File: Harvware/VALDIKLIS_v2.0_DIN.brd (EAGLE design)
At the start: 100 x 86.4 mm, 56 parts, among them IC1 ATMEGA1284, J1 6-3.50, J10 6-3.50, J2 6-3.50, J3 6-3.50, J4 4-3.50, J5 2-3.50, J6 4-3.50, J7 4-3.50, J8 4-3.50, J9 6-3.50, K1 G5V1, K2 G5V1, K3 G5V1, K4 G5V1, Q3 TIP120V, Q4 TIP120V, X12 12MHZ, Y2 16MHz

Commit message: 1
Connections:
- net 0(RX0) renamed D8(RX0)
- net 1(TX0) renamed D9(TX0)
- net 11(MOSI) renamed D5(MOSI)
- net 12(MISO) renamed D6(MISO)
- net 13(SCK) renamed D7(SCK)
- net 16(TDI) renamed D21(TDI)
- net 17(TDO) renamed D20(TDO)
- net 18(TMS) renamed D19(TMS)
- net 19(TCK) renamed D18(TCK)
- net 2(RX1) renamed D10(RX1)
- net 20(SDA) renamed D17(SDA)
- net 21(SCL) renamed D16(SCL)
- net 3(TX1) renamed D11(TX1)
- net A0 renamed A7(31)
- net A1 renamed A6(30)
- net A2 renamed A5(29)
- net A3 renamed A4(28)
- net A4 renamed A3(27)
- net A5 renamed A2(26)
- net A6 renamed A1(25)
- net A7 renamed A0(24)
- net D5 renamed D1
- net D6 renamed D2
- net D7 renamed D3
- removed net D10: IC1.5
- removed net D8: IC1.20
- new net D0: IC1.1
- new net D12: IC1.18
- new net D13: IC1.19
- net D14: now also IC1.20; no longer IC1.29
- net D15: now also IC1.21; no longer IC1.28
- net D22: now also IC1.28; no longer IC1.18
- net D23: now also IC1.29; no longer IC1.21
- net D4: now also IC1.5; no longer IC1.1
- net D9: no longer IC1.19
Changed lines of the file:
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@@
 <contactref element="IC1" pad="9"/>
 </signal>
-<signal name="13(SCK)">
+<signal name="D7(SCK)">
 <contactref element="IC1" pad="8"/>
 </signal>
-<signal name="20(SDA)">
+<signal name="D17(SDA)">
 <contactref element="IC1" pad="23"/>
 </signal>
-<signal name="21(SCL)">
+<signal name="D16(SCL)">
 <contactref element="IC1" pad="22"/>
 </signal>
-<signal name="A4">
+<signal name="A3(27)">
 <contactref element="IC1" pad="37"/>
 </signal>
-<signal name="A5">
+<signal name="A2(26)">
 <contactref element="IC1" pad="38"/>
 </signal>
-<signal name="A0">
+<signal name="A7(31)">
 <contactref element="IC1" pad="33"/>
 </signal>
-<signal name="A1">
+<signal name="A6(30)">
 <contactref element="IC1" pad="34"/>
 </signal>
-<signal name="A2">
+<signal name="A5(29)">
 <contactref element="IC1" pad="35"/>
 </signal>
-<signal name="A3">
+<signal name="A4(28)">
 <contactref element="IC1" pad="36"/>
 </signal>
-<signal name="A6">
+<signal name="A1(25)">
 <contactref element="IC1" pad="39"/>
 </signal>
-<signal name="A7">
+<signal name="A0(24)">
 <contactref element="IC1" pad="40"/>
 </signal>
-<signal name="11(MOSI)">
+<signal name="D5(MOSI)">
 <contactref element="IC1" pad="6"/>
 </signal>
-<signal name="12(MISO)">
+<signal name="D6(MISO)">
 <contactref element="IC1" pad="7"/>
 </signal>
-<signal name="1(TX0)">
+<signal name="D9(TX0)">
 <contactref element="IC1" pad="15"/>
 </signal>
-<signal name="3(TX1)">
+<signal name="D11(TX1)">
 <contactref element="IC1" pad="17"/>
 </signal>
-<signal name="0(RX0)">
+<signal name="D8(RX0)">
 <contactref element="IC1" pad="14"/>
 </signal>
-<signal name="2(RX1)">
+<signal name="D10(RX1)">
 <contactref element="IC1" pad="16"/>
 </signal>
-<signal name="D22">
+<signal name="D12">
 <contactref element="IC1" pad="18"/>
 </signal>
-<signal name="D8">
+<signal name="D0">
+<contactref element="IC1" pad="1"/>
+</signal>
+<signal name="D1">
+<contactref element="IC1" pad="2"/>
+</signal>
+<signal name="D3">
+<contactref element="IC1" pad="4"/>
+</signal>
+<signal name="D4">
+<contactref element="IC1" pad="5"/>
+</signal>
+<signal name="D14">
 <contactref element="IC1" pad="20"/>
 </signal>
-<signal name="D4">
-<contactref element="IC1" pad="1"/>
-</signal>
-<signal name="D5">
-<contactref element="IC1" pad="2"/>
-</signal>
-<signal name="D7">
-<contactref element="IC1" pad="4"/>
-</signal>
-<signal name="D10">
-<contactref element="IC1" pad="5"/>
-</signal>
-<signal name="D14">
-<contactref element="IC1" pad="29"/>
-</signal>
 <signal name="D15">
-<contactref element="IC1" pad="28"/>
-</signal>
-<signal name="16(TDI)">
+<contactref element="IC1" pad="21"/>
+</signal>
+<signal name="D21(TDI)">
 <contactref element="IC1" pad="27"/>
 </signal>
-<signal name="17(TDO)">
+<signal name="D20(TDO)">
 <contactref element="IC1" pad="26"/>
 </signal>
-<signal name="18(TMS)">
+<signal name="D19(TMS)">
 <contactref element="IC1" pad="25"/>
 </signal>
-<signal name="19(TCK)">
+<signal name="D18(TCK)">
 <contactref element="IC1" pad="24"/>
-</signal>
-<signal name="D23">
-<contactref element="IC1" pad="21"/>
 </signal>
 <signal name="AREF">
@@
 </signal>
 <signal name="D9">
-<contactref element="IC1" pad="19"/>
 <contactref element="R9" pad="1"/>
-<wire x1="73.025" y1="68.58" x2="52.07" y2="41.275" width="0" layer="19" extent="1-1"/>
-</signal>
-<signal name="D6">
+</signal>
+<signal name="D2">
 <contactref element="IC1" pad="3"/>
 </signal>
@@
 <wire x1="82.065" y1="5.15" x2="81.28" y2="8.255" width="0" layer="19" extent="1-1"/>
 </signal>
+<signal name="D13">
+<contactref element="IC1" pad="19"/>
+</signal>
+<signal name="D22">
+<contactref element="IC1" pad="28"/>
+</signal>
+<signal name="D23">
+<contactref element="IC1" pad="29"/>
+</signal>
 </signals>

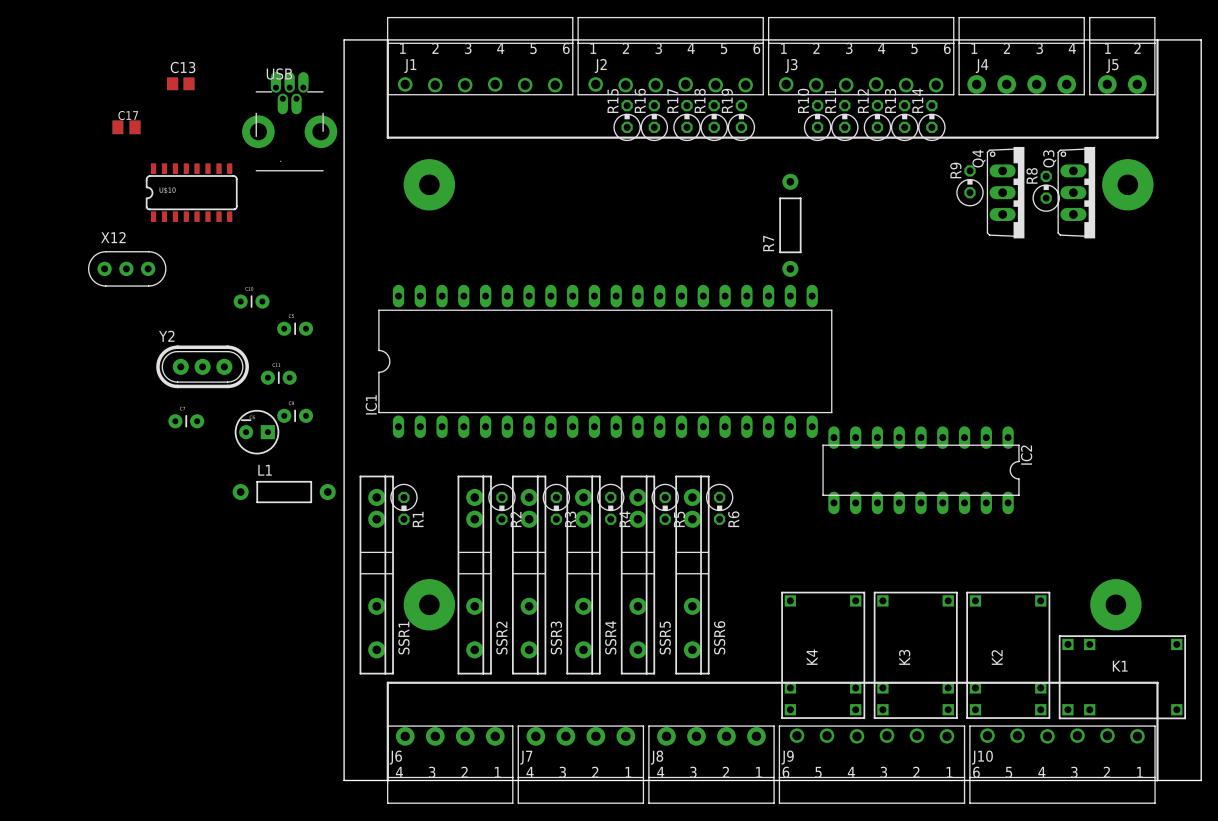
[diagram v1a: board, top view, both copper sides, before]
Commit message: Irškojimai-sprendimai
Relės pakeistos  l293 mikroschema skirta variklių valdymui.
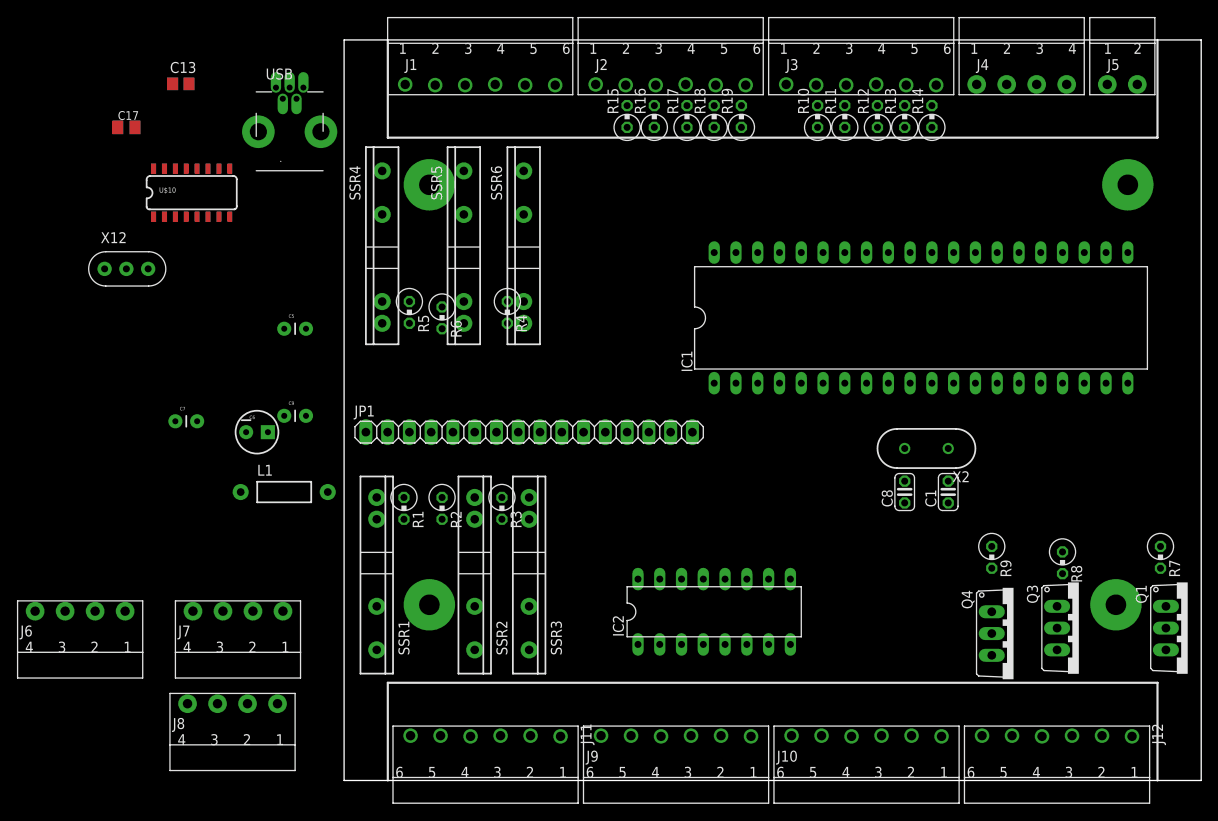
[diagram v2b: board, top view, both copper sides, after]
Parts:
- removed C10, C11: 22p, SparkFun:CAP-PTH-SMALL
- removed K1, K2, K3, K4: G5V1, relay-1:G5V1
- removed Y2: 16MHz, SteveMarple:HC49U-V-RESONATOR
- added C1, C8: 22p, rcl:C025-024X044
- added J11, J12: 6-3.50, con-phoenix-350-1:6-3.50
- added JP1: (no value), pinhead:1X16
- added Q1: TIP120V, rocketfarm:TO220AV
- added X2: 16MHz, SparkFun:HC49US
- IC2: value (none) -> L293D; device uln-udn:DIL18 -> st-microelectronics:DIL16
- R7: value 10k -> (none); device SteveMarple:RES-AXIAL-0.4 -> resistor-1:0309V
- moved R7 58.0 mm to (95.2, 26.0), turned to 270 degrees
- moved J8 56.0 mm to (-5.71, 10.2)
- moved Q4 51.5 mm to (78.1, 17.1)
- moved SSR4 51.4 mm to (4.45, 66.0), turned to 270 degrees
- moved Q3 50.8 mm to (85.7, 17.8)
- moved SSR5 50.0 mm to (14.0, 66.0), turned to 270 degrees
- moved SSR6 49.8 mm to (21.0, 66.0), turned to 270 degrees
- moved J6 45.6 mm to (-23.5, 21.0)
- moved R9 43.9 mm to (75.6, 26.0), turned to 270 degrees
- moved R8 43.9 mm to (83.8, 25.4), turned to 270 degrees
- moved J7 42.6 mm to (-5.08, 21.0)
- moved R6 39.3 mm to (11.4, 54.0)
- moved R5 37.6 mm to (7.62, 54.6)
- moved IC1 37.2 mm to (67.3, 54.0)
- moved IC2 29.2 mm to (43.2, 19.7), turned to 0 degrees
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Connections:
- removed net N$47: J10.5, K2.5, K2.6
- removed net N$52: J10.4, K2.1
- removed net N$55: J10.6, K2.10
- removed net N$56: J10.1, K1.5, K1.6
- removed net N$57: J10.3, K1.1
- removed net N$58: J10.2, K1.10
- removed net N$59: J9.5, K4.5, K4.6
- removed net N$60: J9.4, K4.1
- removed net N$61: J9.6, K4.10
- removed net N$62: J9.2, K3.5, K3.6
- removed net N$63: J9.1, K3.1
- removed net N$64: J9.3, K3.10
- new net +7V: IC2.8
- new net GND2: IC2.5
- new net GND3: IC2.13
- new net GND4: IC2.12
- new net N$65: J12.4, Q3.C
- new net N$66: J12.6, Q4.C
- new net N$67: J12.2, Q1.C
- new net N$68: C1.2, IC1.13, X2.1
- new net N$69: C8.2, IC1.12, X2.2
- new net N$70: IC2.3, J6.2
- new net N$71: IC2.6, J6.1
- net +5V: now also IC2.1, IC2.16
- net GND: now also C1.1, C8.1, IC2.4, J12.1, J12.3, J12.5, Q1.E; no longer C10.2, C11.2, IC2.9, J4.1, J4.3, Y2.GND
- net N$10: now also J11.4, SSR2.DS1; no longer J6.1, SSR2.DS2
- net N$16: now also IC2.2; no longer C11.1, IC1.13, Y2.2
- net N$17: now also IC2.7; no longer C10.1, IC1.12, Y2.1
- net N$19: now also J11.3, SSR2.DS2; no longer J6.2, SSR2.DS1
- net N$2: now also IC2.14, J6.4; no longer IC2.18, K1.9
- net N$21: now also J11.2, SSR3.DS1; no longer J7.3, SSR3.DS2
- net N$22: now also J11.1, SSR3.DS2; no longer J7.4, SSR3.DS1
- net N$23: now also J1.6, SSR6.DS2; no longer J7.2, SSR4.DS1
- net N$24: now also J1.5, SSR6.DS1; no longer J7.1, SSR4.DS2
- net N$25: now also J1.4, SSR5.DS2; no longer J8.4, SSR5.DS1
- net N$26: now also J1.3, SSR5.DS1; no longer J8.3, SSR5.DS2
- net N$27: now also J1.2, SSR4.DS2; no longer J8.2, SSR6.DS1
- net N$28: now also J1.1, SSR4.DS1; no longer J8.1, SSR6.DS2
- net N$3: now also J6.3; no longer IC2.17, K2.2
- net N$4: now also IC2.10; no longer IC2.16, K3.2
- net N$5: no longer K4.2
- net N$6: now also J11.5; no longer J6.3
- net N$7: now also Q1.B, R7.2; no longer J4.2, Q4.C
- net N$8: now also R7.1; no longer J4.4, Q3.C
- net N$9: now also J11.6; no longer J6.4
- net VCC: no longer K1.2, K2.9, K3.9, K4.9
